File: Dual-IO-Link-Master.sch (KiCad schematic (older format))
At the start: 35 parts, among them U2 MAX14819ATM+

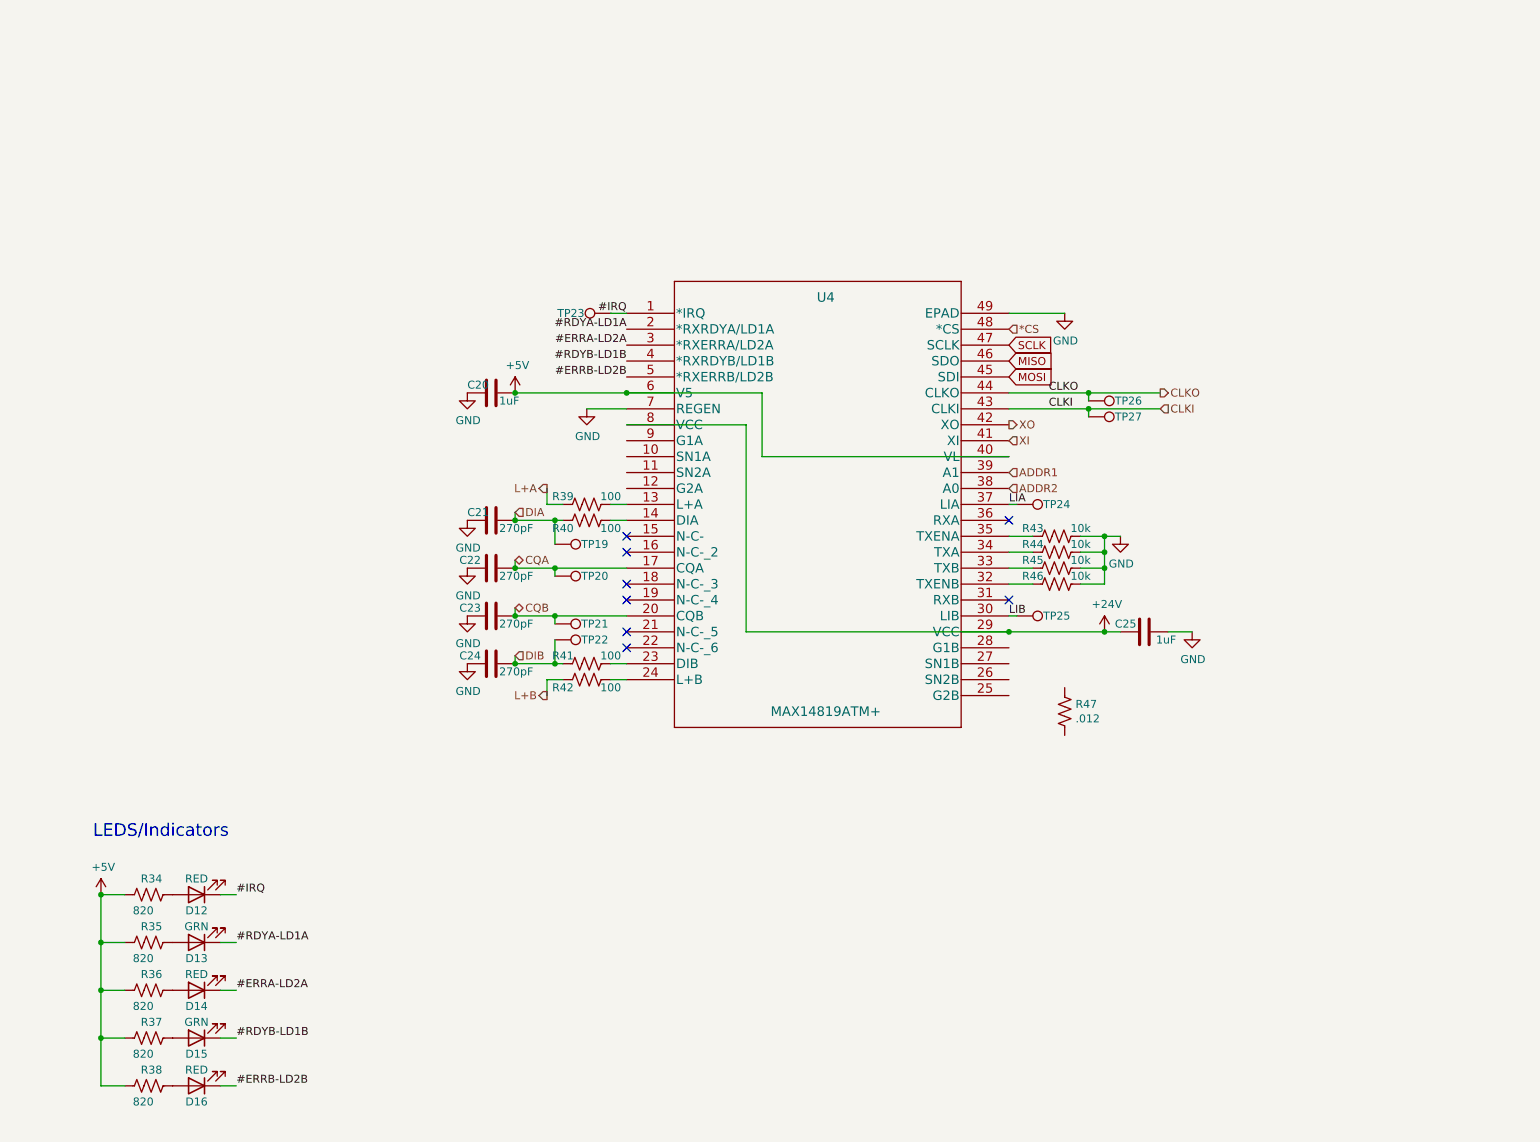
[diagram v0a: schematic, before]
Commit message: New step up that can handle 2A (instead of only 400mA)
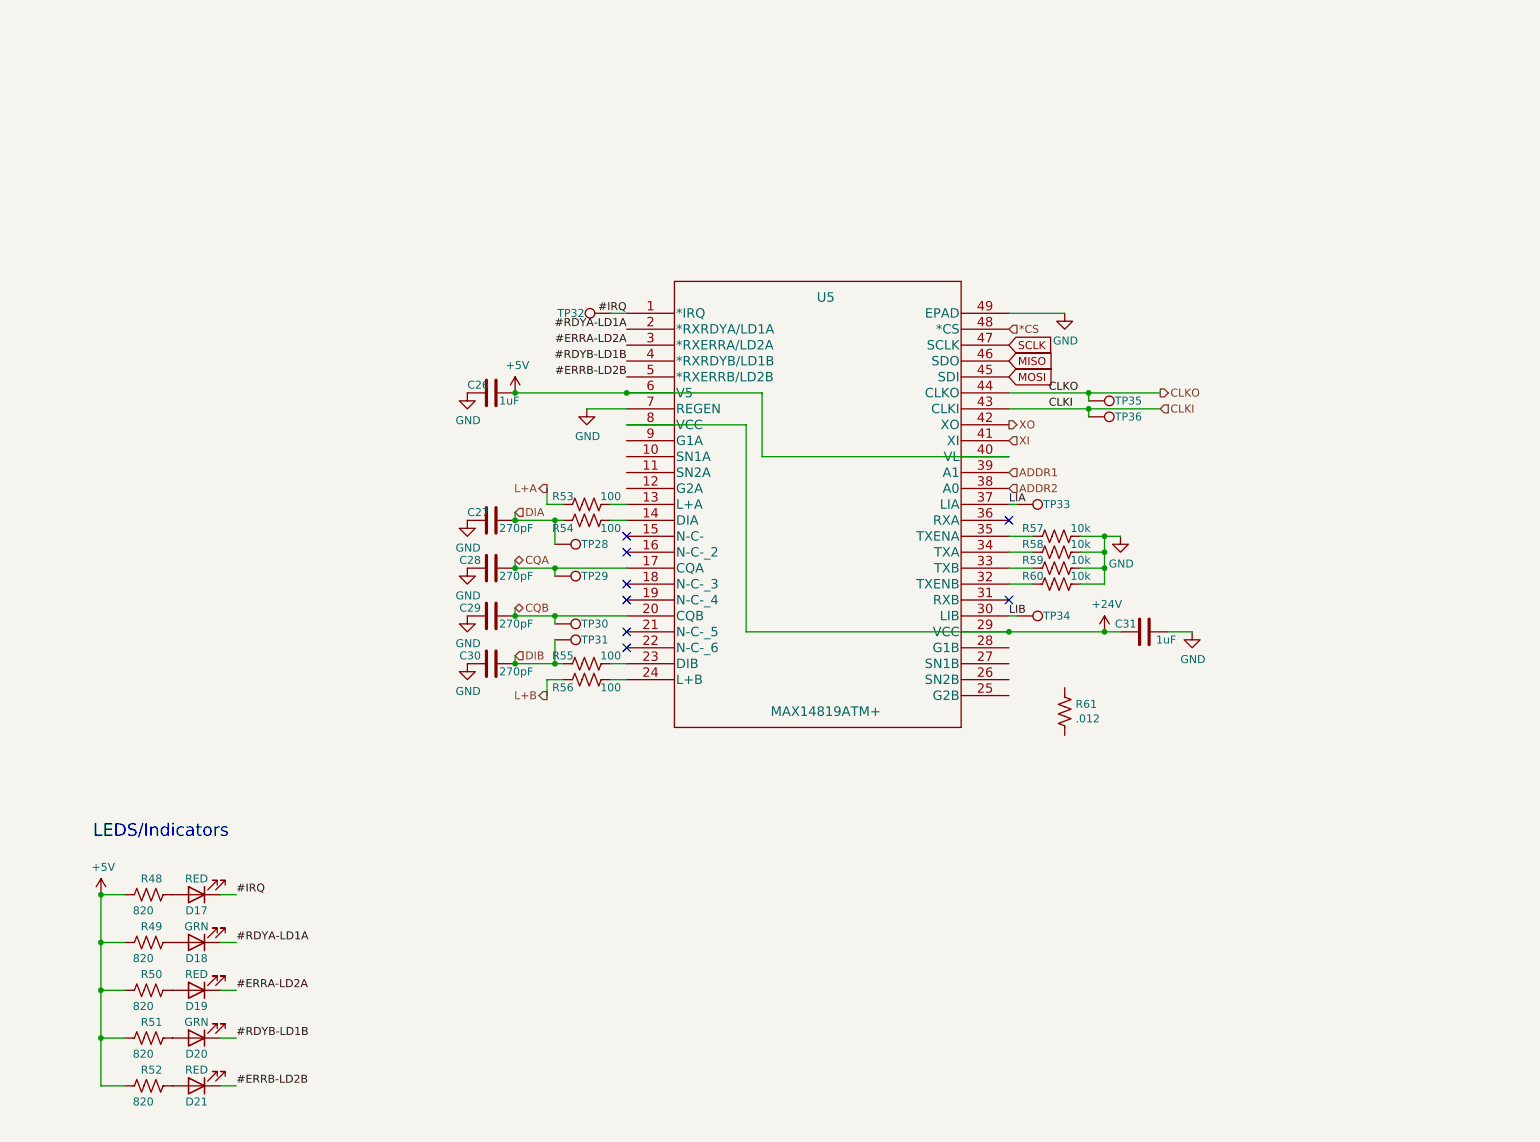
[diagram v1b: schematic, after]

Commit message: Wrapping up schematics for the MAX14819s
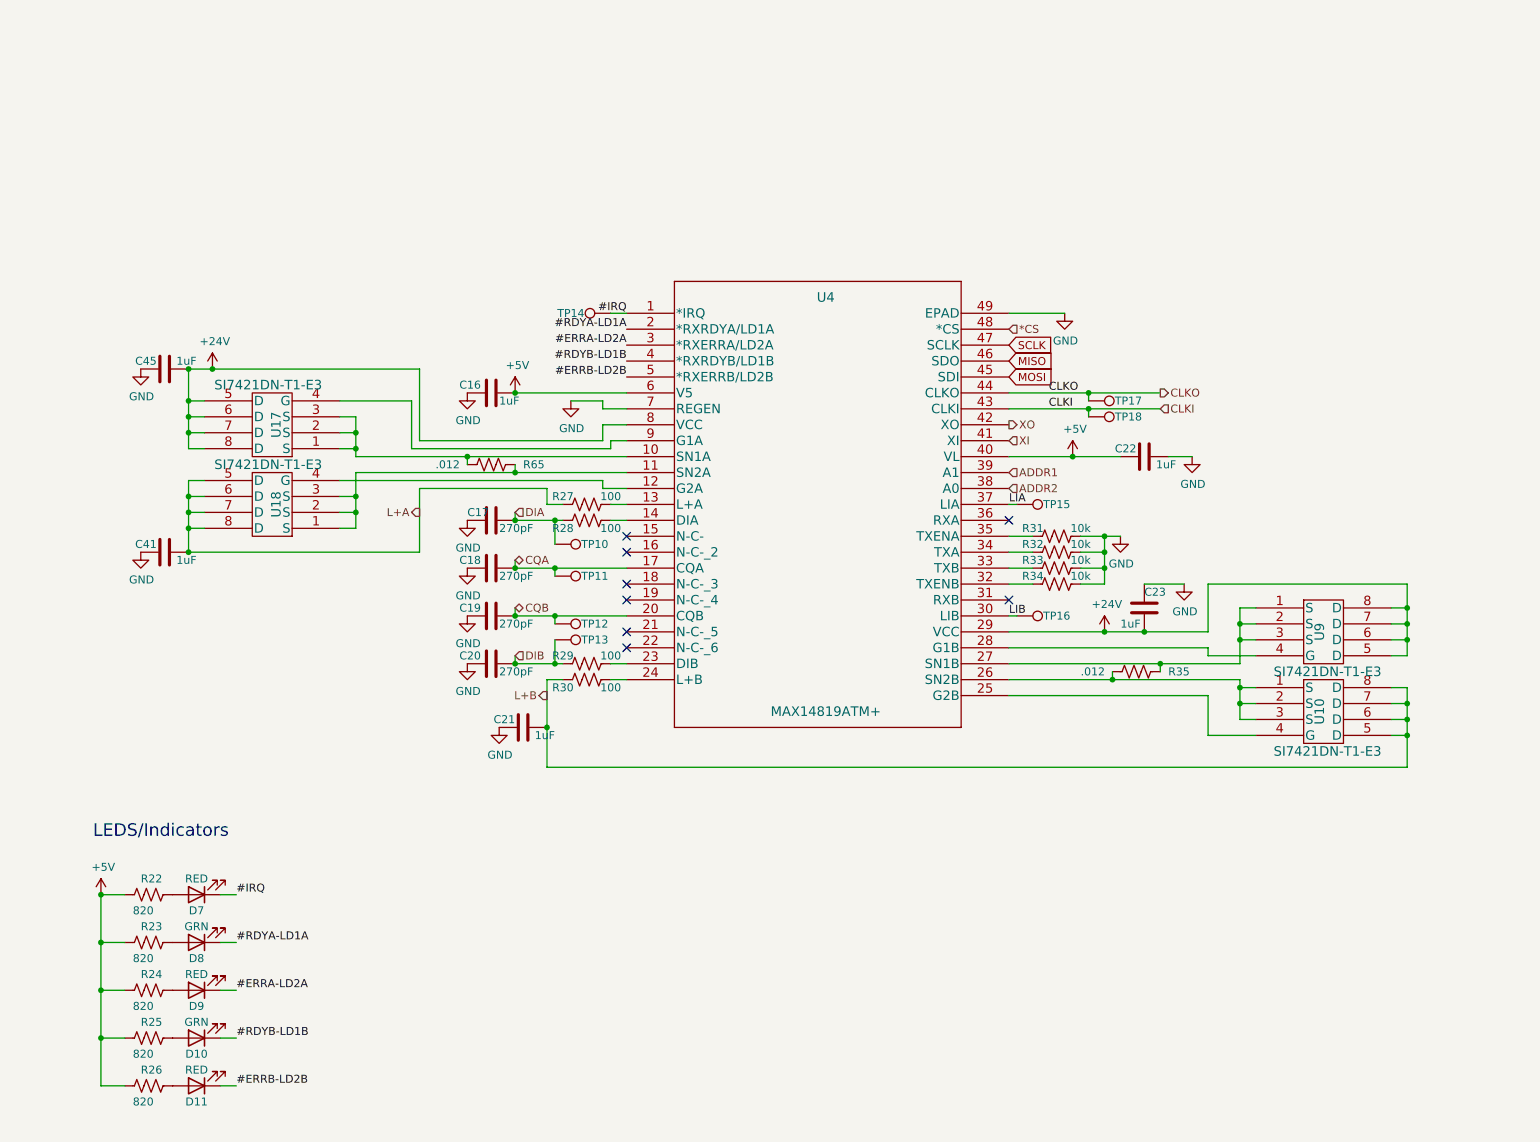
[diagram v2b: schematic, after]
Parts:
- added C13, C14, C40, C44: 1uF, symbol Device:C
- added R64: .012, symbol Device:R_US
- added U10, U17, U18, U9: SI7421DN-T1-E3, MOSFET_4DN-T1-E3_VIS, symbol SI7421DN-T1-E3:SI7421DN-T1-E3
- renumbered C13 to C15, R15 to R10, R16 to R11, R17 to R12, R5 to R13, R6 to R14, R7 to R15, R8 to R16, R9 to R17, R10 to R18, R11 to R19, R12 to R20, R19 to R21, R13 to R8, R14 to R9, TP6 to TP1, TP7 to TP2, TP8 to TP3, TP9 to TP4, TP1 to TP5, TP3 to TP6, TP2 to TP7, TP4 to TP8, TP5 to TP9, U2 to U3
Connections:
- net +24V: now also C15.2, C44.2, U17.5 (D), U17.6 (D), U17.7 (D), U17.8 (D), U9.5 (D), U9.6 (D), U9.7 (D), U9.8 (D); no longer C15.1
- net +5V: now also C14.1
- net GND: now also C15.1, C13.1, C14.2, C40.1, C44.1; no longer C15.2
- net L+A: now also C40.2, U18.5 (D), U18.6 (D), U18.7 (D), U18.8 (D)
- net L+B: now also C13.2, U10.5 (D), U10.6 (D), U10.7 (D), U10.8 (D)
- net at U3.10 (SN1A): now also R64.2, U17.1 (S), U17.2 (S), U17.3 (S)
- net at U3.11 (SN2A): now also R64.1, U18.1 (S), U18.2 (S), U18.3 (S)
- net at U3.12 (G2A): now also U18.4 (G)
- net at U3.25 (G2B): now also U10.4 (G)
- net at U3.26 (SN2B): now also R21.2, U10.1 (S), U10.2 (S), U10.3 (S)
- net at U3.27 (SN1B): now also R21.1, U9.1 (S), U9.2 (S), U9.3 (S)
- net at U3.28 (G1B): now also U9.4 (G)
- net at U3.9 (G1A): now also U17.4 (G)
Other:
- moved on the sheet: C23, R35

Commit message: Schematic edits
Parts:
- added D32: L+A, symbol Device:LED
- added D33: L+B, symbol Device:LED
- added R68, R69: 6.8k, symbol Device:R_US
- added TP37: L+A, symbol Connector:TestPoint
- added TP38: L+B, symbol Connector:TestPoint
- added TVS21, TVS22, TVS23, TVS24, TVS25, TVS26: SMCJ48A, SMCJSeries_LTF, symbol SMCJ48A:SMCJ48A
- D27: renamed from D2; value RED -> IRQ
- D28: renamed from D3; value GRN -> LD1A
- D29: renamed from D4; value RED -> LD2A
- D30: renamed from D5; value GRN -> LD1B
- D31: renamed from D6; value RED -> LD2B
- TP39: renamed from TP1; value TP -> DIA
- TP40: renamed from TP2; value TP -> CQA
- TP41: renamed from TP3; value TP -> CQB
- TP42: renamed from TP4; value TP -> DIB
- TP44: renamed from TP6; value TP -> LIA
- TP45: renamed from TP7; value TP -> LIB
- TP46: renamed from TP8; value TP -> CLKO
- TP47: renamed from TP9; value TP -> CLKI
- renumbered C44 to C42, C40 to C43, C8 to C44, C9 to C45, C10 to C46, C11 to C47, C12 to C48, C13 to C49, C14 to C50, C15 to C51, R8 to R63, R9 to R64, R10 to R65, R11 to R66, R12 to R67, R64 to R70, R13 to R71, R14 to R72, R15 to R73, R16 to R74, R17 to R75, R18 to R76, R19 to R77, R20 to R78, R21 to R79, TP5 to TP43, U3 to U20, U17 to U3, U18 to U4, U9 to U6, U10 to U7
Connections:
- net ADDR1 is gone; now on net GND: U20.39 (A1)
- net ADDR2 is gone; now on net GND: U20.38 (A0)
- net #ERRA-LD2A: now also R65.1; no longer D29.1 (K)
- net #ERRB-LD2B: now also R67.1; no longer D31.1 (K)
- net #IRQ: now also R63.1; no longer D27.1 (K)
- net #RDYA-LD1A: now also R64.1; no longer D28.1 (K)
- net #RDYB-LD1B: now also R66.1; no longer D30.1 (K)
- net +5V: no longer C50.1, R63.2, R64.2, R65.2, R66.2, R67.2, U20.40 (VL)
- net CQA: now also TVS23.2
- net CQB: now also TVS26.2
- net DIA: now also TVS22.2
- net DIB: now also TVS25.2
- net GND: now also R68.1, R69.1
- net L+A: now also D32.2 (A), TP37.1, TVS21.2
- net L+B: now also D33.2 (A), TP38.1, TVS24.2
- net +3V3: now reaches D27.2 (A)
- net +3V3: now also C50.1, D28.2 (A), D29.2 (A), D30.2 (A), D31.2 (A), U20.40 (VL); no longer R63.1
- net LIA: no longer names the net of TP44.1, U20.37 (LIA)
- net LIB: no longer names the net of TP45.1, U20.30 (LIB)
- new net: D32.1 (K), R68.2
- new net: D33.1 (K), R69.2
- new net: D27.1 (K), R63.2
- new net: D28.1 (K), R64.2
- new net: D29.1 (K), R65.2
- new net: D30.1 (K), R66.2
- new net: D31.1 (K), R67.2
- new net TVS_CLAMP: TVS21.1, TVS22.1, TVS23.1, TVS24.1, TVS25.1, TVS26.1
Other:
- note added: "IO-Link Master\n"
- note added: "LEDs/Indicators"
- note added: "TVS"
- note removed: "LEDS/Indicators"
- moved on the sheet: C43, D27, D28, D29, D30, D31, R63, R64, R65, R66, R67, TP41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
